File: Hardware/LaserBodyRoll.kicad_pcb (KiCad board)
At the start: 2 copper layers, 100 x 32 mm, 74 parts, among them J1 FTSH-105-01-L-DV-K, J2 Conn_02x13_Odd_Even, J3 Conn_01x08, Q1 Q_NPN_BCE, U1 AOZ1280CI, U2 STM32F303RETx, U3 LMC6032, U4 TJA1051T-3, U5 ITS42K5D, U6 ICM-20602, U7 VL53L0X, Y1 8MHz, Y2 32.768

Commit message: Working on a redesigned board.
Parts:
- removed C4, C5: 20p, Capacitors_SMD:C_0603
- removed C7, C8: 6.8p, Capacitors_SMD:C_0603
- removed R4, R5, R6, R7: 0, Resistors_SMD:R_0603
- removed Y1: 8MHz, Crystals:Crystal_SMD_MicroCrystal_CC4V-T1A-2pin_5.0x1.9mm_HandSoldering
- removed Y2: 32.768, Crystals:Crystal_SMD_MicroCrystal_CC7V-T1A-2pin_3.2x1.5mm_HandSoldering
- added C24: 0.1u, Capacitors_SMD:C_0603, F.Cu at (109.8, 42.2)
- added C25: 2.2U, Capacitors_SMD:C_0603, F.Cu at (115.8, 45.2)
- added C26: 10n, Capacitors_SMD:C_0603, F.Cu at (113.8, 45.2)
- added C27: 4.7u, Capacitors_SMD:C_0603, F.Cu at (109.8, 44.0)
- C10: moved to F.Cu
- C16, C17, C22: value 10n -> 0.1u
- C20: value 0.1u -> 10n
- C21: value 2.2U -> 10n
- C23: value 4.7u -> 0.1u
- C6: footprint KicadFootprint:Elna_Dynacap -> Capacitors_SMD:C_1206_HandSoldering
- J1, TP1, TP2, TP3: moved to B.Cu
- moved D4 71.3 mm to (90.5, 53.2), turned to 180 degrees
- moved C6 66.2 mm to (91.8, 47.8), turned to 90 degrees
- moved R3 61.4 mm to (90.8, 55.5), turned to 0 degrees
- moved C10 50.1 mm to (90.8, 57.2), turned to 180 degrees
- moved C22 46.6 mm to (118.0, 45.2)
- moved J2 46.1 mm to (110.1, 62.5)
- moved R24 43.3 mm to (110.8, 51.0), turned to 180 degrees
- moved U6 43.0 mm to (116.8, 49.2)
- moved TP3 41.5 mm to (108.8, 58.4)
- moved R23 40.4 mm to (110.8, 53.2), turned to 180 degrees
- moved C23 35.6 mm to (114.5, 52.8), turned to 180 degrees
- moved TP2 34.3 mm to (104.8, 58.4)
- moved C17 34.0 mm to (71.2, 66.0), turned to 180 degrees
- moved R12 32.4 mm to (73.2, 44.2), turned to 0 degrees
- moved R11 31.8 mm to (73.2, 42.5), turned to 0 degrees
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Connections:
- C18 pad 2: GND -> Net-(C17-Pad1)
- C19 pad 1: VCC -> Net-(C19-Pad1)
- C19 pad 2: GND -> Net-(C16-Pad1)
- C20 pad 1: VCC -> Net-(C18-Pad1)
- C21 pad 1: VCC -> Net-(C19-Pad1)
- C22 pad 1: VCC -> Net-(C22-Pad1)
- D6 pad 1: Net-(C16-Pad1) -> Net-(C18-Pad1)
- D7 pad 1: Net-(C17-Pad1) -> Net-(C19-Pad1)
- J2 pad 16: BCM23 -> (no net)
- R13 pad 1: Net-(R13-Pad1) -> Net-(C16-Pad1)
- R14 pad 1: Net-(R14-Pad1) -> Net-(C17-Pad1)
- R15 pad 1: Net-(R14-Pad1) -> Net-(C17-Pad1)
- R15 pad 2: Net-(C16-Pad1) -> Net-(C18-Pad1)
- R16 pad 1: Net-(R13-Pad1) -> Net-(C16-Pad1)
- R16 pad 2: Net-(C17-Pad1) -> Net-(C19-Pad1)
- R18 pad 2: Net-(C17-Pad1) -> Net-(C19-Pad1)
- R19 pad 2: Net-(C16-Pad1) -> Net-(C18-Pad1)
- U2 pad 16: (no net) -> BCM24
- U2 pad 25: CPU_DIN1 -> (no net)
- U2 pad 26: Net-(R8-Pad2) -> (no net)
- U2 pad 27: Net-(R9-Pad2) -> (no net)
- U2 pad 28: Net-(R10-Pad2) -> (no net)
- U2 pad 29: BCM24 -> (no net)
- U2 pad 3: Net-(R6-Pad1) -> CPU_DIN1
- U2 pad 30: IMU_INT -> (no net)
- U2 pad 37: (no net) -> Net-(R8-Pad2)
- U2 pad 38: (no net) -> Net-(R9-Pad2)
- U2 pad 39: (no net) -> Net-(R10-Pad2)
- U2 pad 4: Net-(R7-Pad1) -> (no net)
- U2 pad 43: CAN_TXD -> (no net)
- U2 pad 44: CAN_RXD -> (no net)
- U2 pad 45: (no net) -> IMU_INT
- U2 pad 5: Net-(R4-Pad1) -> (no net)
- U2 pad 6: Net-(R5-Pad1) -> (no net)
- U2 pad 61: (no net) -> CAN_RXD
- U2 pad 62: BCM23 -> CAN_TXD
- U3 pad 1: Net-(C17-Pad1) -> Net-(C19-Pad1)
- U3 pad 2: Net-(R13-Pad1) -> Net-(C16-Pad1)
- U3 pad 6: Net-(R14-Pad1) -> Net-(C17-Pad1)
- U3 pad 7: Net-(C16-Pad1) -> Net-(C18-Pad1)
- U6 pad 14: Net-(C18-Pad1) -> Net-(C22-Pad1)
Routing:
- net 5V: track 0.00 -> 55.6 mm, vias 0 -> 1
- net SDA: track 0.00 -> 39.5 mm, vias 0 -> 1
- net SCL: track 0.00 -> 36.8 mm, vias 0 -> 4
- net PI_NSS: track 0.00 -> 32.2 mm
- net PI_MISO: track 0.00 -> 31.2 mm
- net PI_CLK: track 0.00 -> 29.5 mm
- net PI_MOSI: track 0.00 -> 25.3 mm, vias 0 -> 1
- net 12V: track 0.00 -> 24.3 mm, vias 0 -> 2
- net IMU_INT: track 0.00 -> 12.4 mm, vias 0 -> 2
- net BCM24: track 0.00 -> 11.6 mm, vias 0 -> 1
- net CAN_RXD: track 0.00 -> 10.9 mm, vias 0 -> 2
- net /IO/CANH: track 0.00 -> 9.72 mm
- net Net-(R8-Pad2): track 0.00 -> 8.31 mm
- net /IO/CANL: track 0.00 -> 7.99 mm, vias 0 -> 1
- net /IO/12V_PULLUP: track 0.00 -> 7.85 mm
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- added copper zone on F.Cu, net Net-(C2-Pad1)
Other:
- board size 100 x 32 mm -> 65 x 30 mm

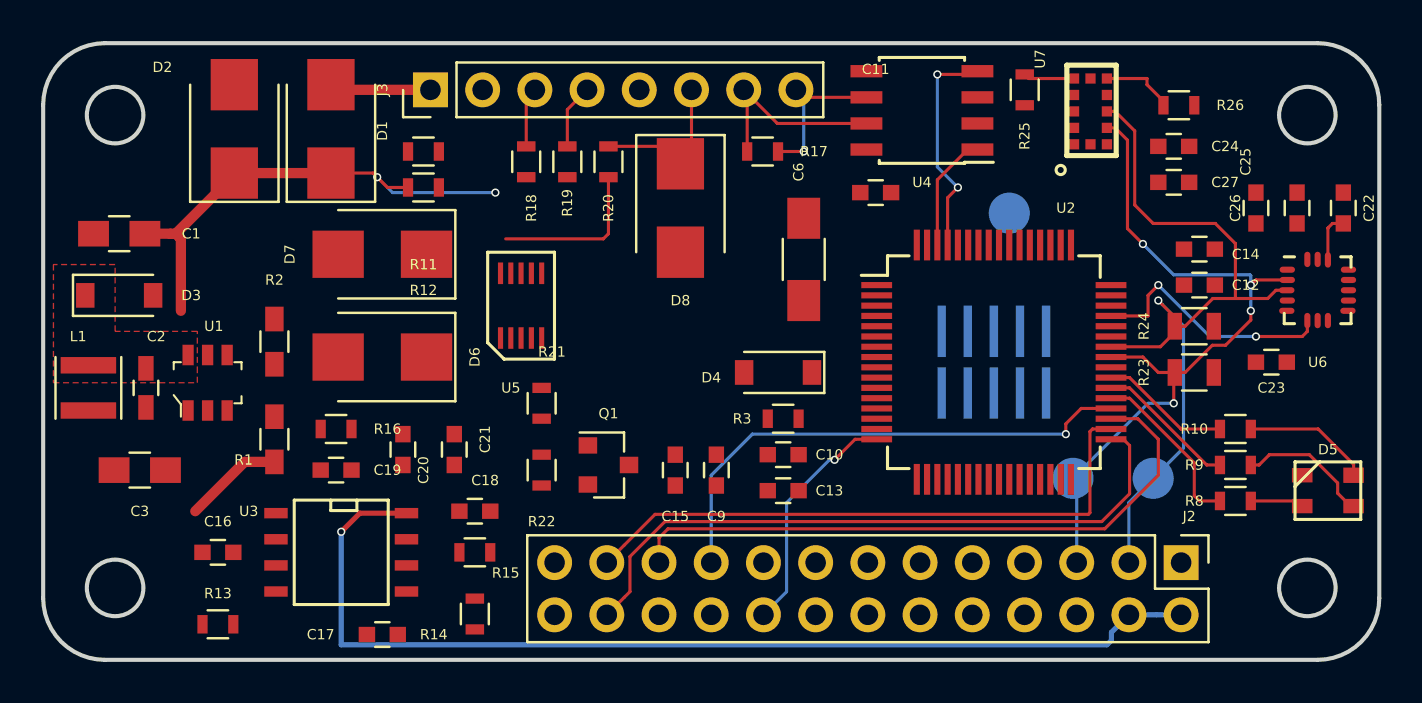
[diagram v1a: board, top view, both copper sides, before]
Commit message: Big refactor, got rid of all software. Everything will run on the Pi.
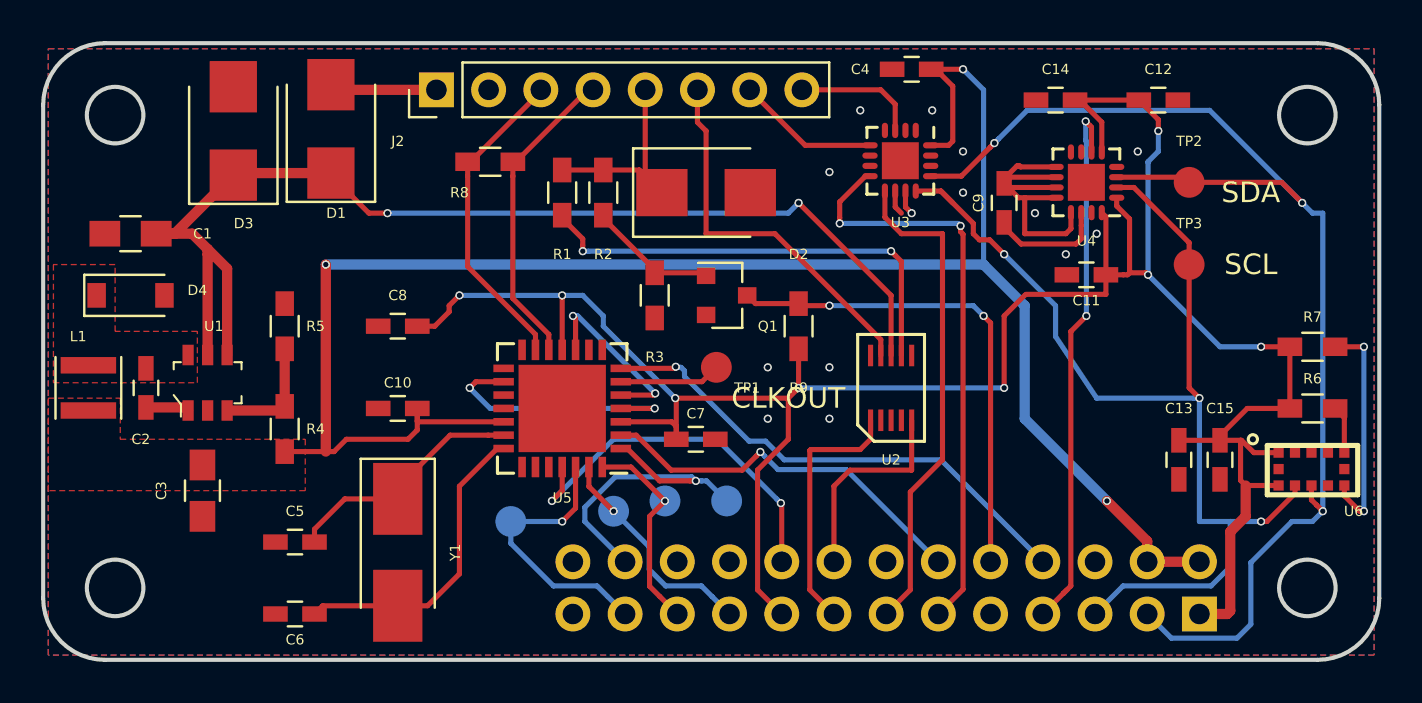
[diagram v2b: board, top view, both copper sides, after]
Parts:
- removed C16, C17, C18, C19, C22, C23, C24: 0.1u, Capacitors_SMD:C_0603
- removed C20, C21, C26: 10n, Capacitors_SMD:C_0603
- removed C25: 2.2U, Capacitors_SMD:C_0603
- removed C27: 4.7u, Capacitors_SMD:C_0603
- removed D5: CLV1L-FKB, KicadFootprint:CREE_PLCC4
- removed D6, D7: D_Zener, Diodes_SMD:D_SMB
- removed D8: D_TVS, Diodes_SMD:D_SMB
- removed J3: Conn_01x08, Pin_Headers:Pin_Header_Straight_1x08_Pitch2.54mm
- removed R10: 330, Resistors_SMD:R_0603
- removed R11, R25, R26: 10k, Resistors_SMD:R_0603
- removed R12: 75k, Resistors_SMD:R_0603
- removed R13, R14: 44.2k, Resistors_SMD:R_0603
- removed R15, R16, R18, R19, R20, R21, R22: 24.3k, Resistors_SMD:R_0603
- removed R17: 120, Resistors_SMD:R_0603
- removed R23, R24: 1.7k, Resistors_SMD:R_0805
- removed U7: VL53L0X, KicadFootprint:VL53L0x
- added C4: 0.1u, Capacitors_SMD:C_0603_HandSoldering, F.Cu at (97.0, 38.5)
- added C5: 22p, Capacitors_SMD:C_0603_HandSoldering, F.Cu at (67.0, 61.5)
- added C7: 0.1u, Capacitors_SMD:C_0603_HandSoldering, F.Cu at (86.5, 56.5)
- added C8: 0.1u, Capacitors_SMD:C_0603_HandSoldering, F.Cu at (72.0, 51.0)
- added R4: 49.9k, Resistors_SMD:R_0603_HandSoldering, F.Cu at (66.5, 56.0)
- added R5: 9.53k, Resistors_SMD:R_0603_HandSoldering, F.Cu at (66.5, 51.0)
- added R6: 10k, Resistors_SMD:R_0603_HandSoldering, F.Cu at (116.5, 55.0)
- added R7: 10k, Resistors_SMD:R_0603_HandSoldering, F.Cu at (116.5, 52.0)
- added TP4: TestPoint, Measurement_Points:Measurement_Point_Round-SMD-Pad_Small, B.Cu at (77.5, 60.5)
- added TP5: TestPoint, Measurement_Points:Measurement_Point_Round-SMD-Pad_Small, B.Cu at (82.5, 60.0)
- added TP6: TestPoint, Measurement_Points:Measurement_Point_Round-SMD-Pad_Small, B.Cu at (85.0, 59.5)
- added TP7: TestPoint, Measurement_Points:Measurement_Point_Round-SMD-Pad_Small, B.Cu at (88.0, 59.5)
- added Y1: 16MHz, Crystals:Crystal_SMD_5032-2pin_5.0x3.2mm_HandSoldering, F.Cu at (72.0, 62.0)
- C10, C11, C13: value 100n -> 0.1u; footprint Capacitors_SMD:C_0603 -> Capacitors_SMD:C_0603_HandSoldering
- C12: value 100n -> 2.2U; footprint Capacitors_SMD:C_0603 -> Capacitors_SMD:C_0603_HandSoldering
- C14: value 1u -> 10n; footprint Capacitors_SMD:C_0603 -> Capacitors_SMD:C_0603_HandSoldering
- C15: value 10n -> 4.7u; footprint Capacitors_SMD:C_0603 -> Capacitors_SMD:C_0603_HandSoldering
- C6: value 1.5F -> 22p; footprint Capacitors_SMD:C_1206_HandSoldering -> Capacitors_SMD:C_0603_HandSoldering
- C9: value 4.7u -> 0.1u; footprint Capacitors_SMD:C_0603 -> Capacitors_SMD:C_0603_HandSoldering
- D3: value D_Schottky -> D_TVS; footprint Diodes_SMD:D_SOD-123 -> Diodes_SMD:D_SMB
- D4: value D -> D_Schottky
- J1: value FTSH-105-01-L-DV-K -> Conn_02x13_Odd_Even; footprint KicadFootprint:FTSH-105-01-L-DV-K -> Pin_Headers:Pin_Header_Straight_2x13_Pitch2.54mm
- J2: value Conn_02x13_Odd_Even -> Conn_01x08; footprint Pin_Headers:Pin_Header_Straight_2x13_Pitch2.54mm -> Pin_Headers:Pin_Header_Straight_1x08_Pitch2.54mm
- R1: value 49.9k -> 24.3k
- R2: value 9.53k -> 24.3k
- R3: value 25 -> 24.3k; footprint Resistors_SMD:R_0603 -> Resistors_SMD:R_0603_HandSoldering
- R8: value 330 -> 120; footprint Resistors_SMD:R_0603 -> Resistors_SMD:R_0603_HandSoldering
- R9: value 330 -> 1k; footprint Resistors_SMD:R_0603 -> Resistors_SMD:R_0603_HandSoldering
- TP1, TP2, TP3: value Test_Point -> TestPoint; footprint Connectors_TestPoints:Test_Point_Pad_d2.0mm -> Measurement_Points:Measurement_Point_Round-SMD-Pad_Small; moved to F.Cu
- U2: value STM32F303RETx -> ITS42K5D; footprint Housings_QFP:TQFP-64_10x10mm_Pitch0.5mm -> KicadFootprint:PG-TSON-10
- U3: value LMC6032 -> MCP47X; footprint SMD_Packages:SOIC-8-N -> Housings_DFN_QFN:QFN-16-1EP_3x3mm_Pitch0.5mm
- U4: value TJA1051T-3 -> ICM-20602; footprint Housings_SOIC:SOIC-8_3.9x4.9mm_Pitch1.27mm -> Housings_DFN_QFN:QFN-16-1EP_3x3mm_Pitch0.5mm
- U5: value ITS42K5D -> MCP25625; footprint KicadFootprint:PG-TSON-10 -> Housings_DFN_QFN:QFN-28-1EP_6x6mm_Pitch0.65mm
- U6: value ICM-20602 -> VL53L0X; footprint KicadFootprint:QFN-16-no_center_3x3mm_Pitch0.5mm -> KicadFootprint:VL53L0x
- moved J2 42.9 mm to (73.9, 39.5), turned to 90 degrees
- moved R8 39.8 mm to (76.5, 43.0), turned to 0 degrees
- moved U3 33.2 mm to (96.5, 43.0)
- moved D4 31.7 mm to (59.0, 49.5), turned to 0 degrees
- moved C6 30.2 mm to (67.0, 65.0), turned to 180 degrees
- moved C15 26.5 mm to (112.0, 57.5)
- moved D2 23.2 mm to (87.0, 44.5), turned to 0 degrees
- moved R9 22.3 mm to (91.5, 51.0), turned to 90 degrees
- moved C13 19.3 mm to (110.0, 57.5), turned to 270 degrees
- moved C9 19.1 mm to (101.5, 45.0), turned to 90 degrees
- moved C10 18.9 mm to (72.0, 55.0), turned to 0 degrees
- moved R1 18.4 mm to (80.0, 44.5), turned to 270 degrees
- moved R2 17.6 mm to (82.0, 44.5), turned to 270 degrees
- moved TP1 16.1 mm to (87.5, 53.0), turned to 90 degrees
- moved J1 15.8 mm to (111.0, 65.0), turned to 90 degrees
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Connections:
- C10 pad 1: VCC -> GND
- C10 pad 2: GND -> +5V
- C3 pad 1: 5V -> +5V
- C9 pad 1: VCC -> Net-(C9-Pad1)
- D2 pad 1: 12V -> /DIN
- D3 pad 1: Net-(C2-Pad1) -> 12V
- D4 pad 1: Net-(C6-Pad1) -> Net-(C2-Pad1)
- D4 pad 2: Net-(D4-Pad2) -> GND
- J1 pad 10: /Processor/STM_RES -> BCM15
- J1 pad 2: /Processor/STM_SWDIO -> +5V
- J1 pad 3: GND -> SDA
- J1 pad 4: /Processor/STM_SWDCLK -> +5V
- J1 pad 5: GND -> SCL
- J1 pad 6: (no net) -> GND
- J1 pad 7: GND -> BCM4
- J1 pad 8: (no net) -> BCM14
- J2 pad 1: VCC -> VIN
- J2 pad 2: 5V -> GND
- J2 pad 3: SDA -> /CANH
- J2 pad 4: 5V -> /CANL
- J2 pad 5: SCL -> /DIN
- J2 pad 6: GND -> /DOUT
- J2 pad 7: (no net) -> /ANA_OUT2
- J2 pad 8: (no net) -> /ANA_OUT1
- L1 pad 2: 5V -> +5V
- Q1 pad 3: CPU_DIN1 -> BCM15
- R1 pad 1: 5V -> /DIN
- R1 pad 2: Net-(R1-Pad2) -> /12V_PULLUP
- R2 pad 1: Net-(R1-Pad2) -> /DIN
- R2 pad 2: GND -> Net-(Q1-Pad1)
- R3 pad 1: Net-(D4-Pad2) -> Net-(Q1-Pad1)
- R3 pad 2: VCC -> GND
- R8 pad 1: Net-(D5-Pad2) -> /CANH
- R8 pad 2: Net-(R8-Pad2) -> /CANL
- R9 pad 1: Net-(D5-Pad3) -> VCC
- R9 pad 2: Net-(R9-Pad2) -> BCM15
- TP1 pad 1: /Processor/STM_RES -> Net-(TP1-Pad1)
- TP2 pad 1: SCL -> SDA
- TP3 pad 1: SDA -> SCL
- U1 pad 3: Net-(R1-Pad2) -> Net-(R4-Pad2)
- U2 pad 1: Net-(C6-Pad1) -> BCM22
- U2 pad 10: CPU_DOUT2 -> GND
- U2 pad 2: (no net) -> Net-(U2-Pad2)
- U2 pad 3: CPU_DIN1 -> GND
- U2 pad 4: (no net) -> Net-(U2-Pad4)
- U2 pad 5: (no net) -> BCM23
- U2 pad 6: (no net) -> GND
- U2 pad 7: /Processor/STM_RES -> /12V_PULLUP
- U2 pad 8: CPU_DOUT1 -> 12V
- U2 pad 9: CPU_DOUT1_ST -> /DOUT
- U3 pad 1: Net-(C19-Pad1) -> GND
- U3 pad 3: DAC1 -> /ANA_OUT1
- U3 pad 4: GND -> Net-(U3-Pad4)
- U3 pad 5: DAC2 -> /ANA_OUT2
- U3 pad 8: 5V -> BCM17
- U4 pad 1: CAN_TXD -> VCC
- U4 pad 2: GND -> SCL
- U4 pad 3: 5V -> SDA
- U4 pad 4: CAN_RXD -> GND
- U4 pad 6: /IO/CANL -> BCM4
- U4 pad 7: /IO/CANH -> Net-(U4-Pad7)
- U4 pad 8: GND -> Net-(U4-Pad8)
- U5 pad 1: CPU_DOUT1 -> PI_NSS
- U5 pad 10: GND -> Net-(U5-Pad10)
- U5 pad 2: CPU_DOUT1_ST -> BCM18
- U5 pad 3: GND -> VCC
- U5 pad 4: CPU_DOUT2 -> Net-(U5-Pad16)
- U5 pad 5: CPU_DOUT2_ST -> Net-(U5-Pad10)
- U5 pad 6: GND -> Net-(TP1-Pad1)
- U5 pad 7: /IO/12V_PULLUP -> BCM14
- U5 pad 8: 12V -> Net-(U5-Pad8)
- U5 pad 9: /IO/DOUT -> Net-(U5-Pad9)
- U6 pad 10: GND -> SCL
- U6 pad 11: GND -> VCC
- U6 pad 2: SCL -> GND
- U6 pad 3: SDA -> GND
- U6 pad 5: VCC -> /VL53L0X_XSHUT
- U6 pad 6: IMU_INT -> GND
- U6 pad 7: (no net) -> /VL53L0X_GP
- U6 pad 8: (no net) -> Net-(U6-Pad8)
- U6 pad 9: GND -> SDA
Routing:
- net VCC: track 0.00 -> 120.4 mm, vias 0 -> 8
- net +5V: track 0.00 -> 90.9 mm, vias 0 -> 3
- net 5V: track 55.6 -> 0.00 mm, vias 1 -> 0
- net 12V: track 24.3 -> 56.3 mm
- net BCM17: track 0.00 -> 28.4 mm, vias 0 -> 2
- net BCM4: track 0.00 -> 26.7 mm, vias 0 -> 2
- net BCM14: track 0.00 -> 24.7 mm, vias 0 -> 1
- net BCM27: track 0.00 -> 24.0 mm
- net BCM15: track 0.00 -> 24.0 mm, vias 0 -> 2
- net /12V_PULLUP: track 0.00 -> 22.4 mm, vias 0 -> 2
- net SDA: track 39.5 -> 61.3 mm, vias 1 -> 3
- net PI_MISO: track 31.2 -> 10.1 mm, vias 0 -> 1
- net BCM18: track 0.00 -> 18.7 mm, vias 0 -> 1
- net /DOUT: track 0.00 -> 18.6 mm
- net GND: track 0.00 -> 18.4 mm, vias 0 -> 14
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- added copper zone on F.Cu, net +5V
- added copper zone on B.Cu, net GND
- added copper zone on F.Cu, net GND
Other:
- board text added: "CLKOUT"
- board text added: "CS"
- board text added: "LaserBodyRoll Rev D Copyright Nick Butts 2019"
- board text added: "MISO"
- board text added: "MOSI"
- board text added: "SCL"
- board text added: "SCLK"
- board text added: "SDA"
- board text removed: "LaserBodyRoll Rev C Copyright Nick Butts 2018"

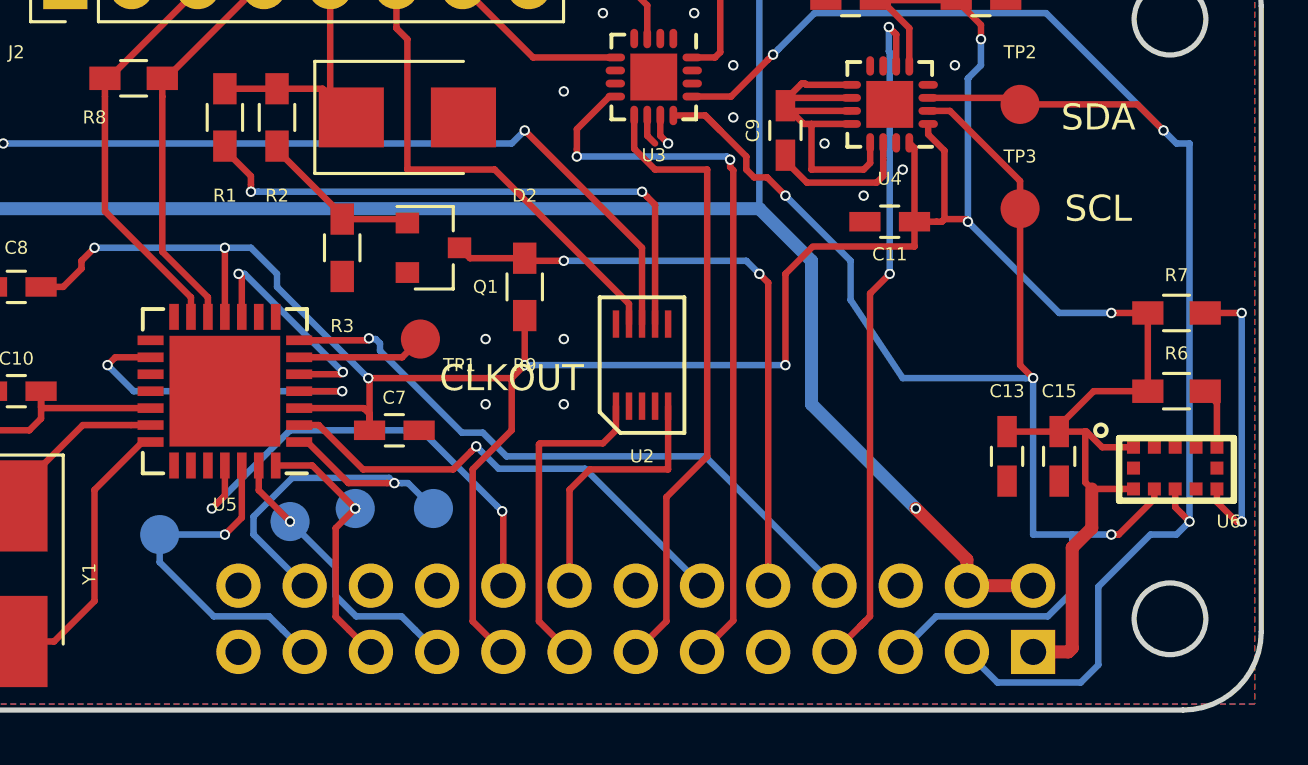
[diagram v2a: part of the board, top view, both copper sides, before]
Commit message: Added an LDO to power this board.
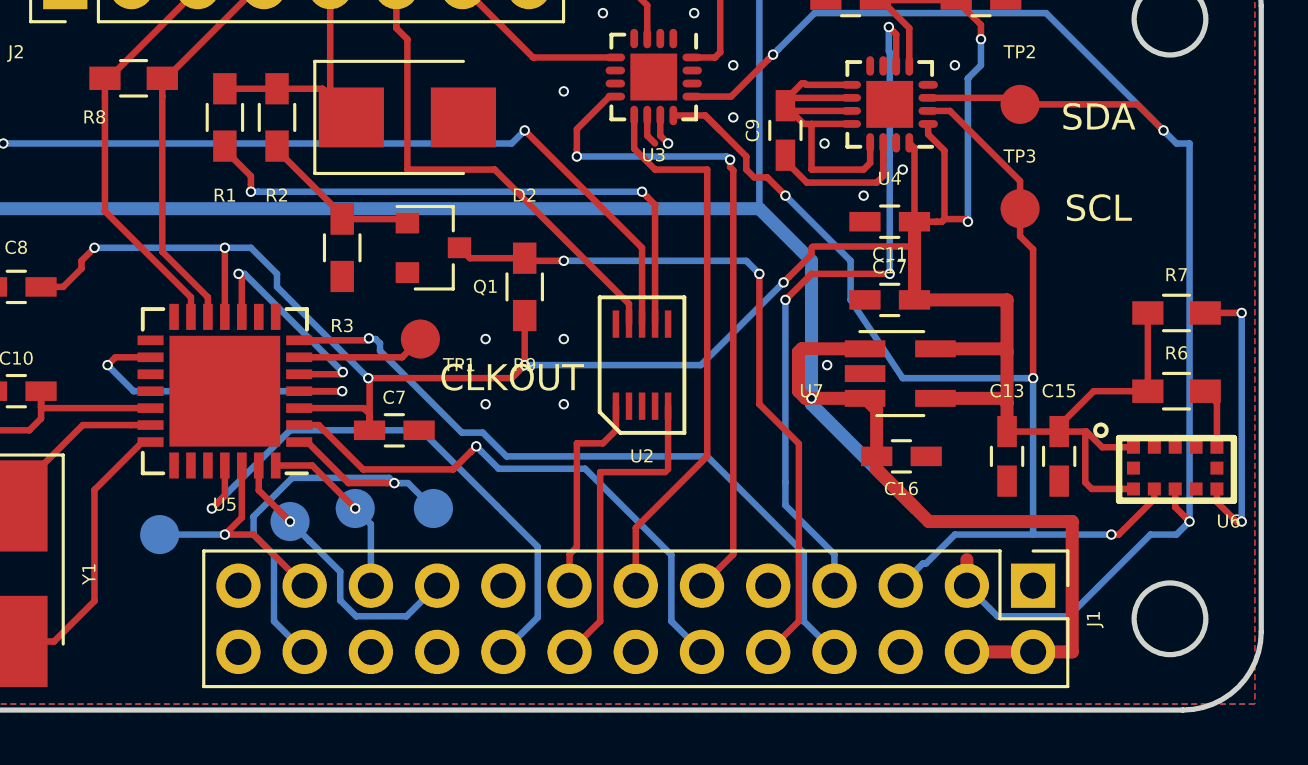
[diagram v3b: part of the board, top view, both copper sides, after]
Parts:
- added C16: 0.1u, Capacitors_SMD:C_0603_HandSoldering, F.Cu at (106.0, 57.5)
- added C17: 0.1u, Capacitors_SMD:C_0603_HandSoldering, F.Cu at (105.5, 51.5)
- added U7: LD3985, TO_SOT_Packages_SMD:SOT-23-5_HandSoldering, F.Cu at (105.9, 54.3)
- J1: moved to F.Cu
- moved J1 2.54 mm to (111.0, 62.5), turned to 270 degrees
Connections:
- J1 pad 1: VCC -> Net-(J1-Pad1)
- J1 pad 17: VCC -> Net-(J1-Pad17)
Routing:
- net +5V: track 90.9 -> 111.6 mm
- net VCC: track 120.4 -> 107.7 mm, vias 8 -> 7
- net BCM22: track 12.5 -> 8.21 mm
- net PI_CLK: track 13.5 -> 9.29 mm
- net SCL: track 54.1 -> 50.2 mm
- net BCM24: track 18.4 -> 22.0 mm, vias 2 -> 1
- net BCM15: track 24.0 -> 27.5 mm
- net PI_MISO: track 10.1 -> 6.94 mm
- net BCM14: track 24.7 -> 27.3 mm
- net PI_NSS: track 15.8 -> 18.3 mm
- net BCM27: track 24.0 -> 21.5 mm
- net BCM18: track 18.7 -> 21.3 mm
- net BCM17: track 28.4 -> 25.9 mm
- net BCM23: track 10.2 -> 12.3 mm
- net SDA: track 61.3 -> 59.5 mm
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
